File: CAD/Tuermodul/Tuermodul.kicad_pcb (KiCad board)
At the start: 2 copper layers, 206.1 x 101.6 mm, 174 parts, among them J101 Conn_02x16_Counter_Clockwise, J201 Conn_02x20_Odd_Even, J202 Conn_02x01, J203 Conn_02x01, J204 Conn_02x01, J205 Conn_02x01, J301 Conn_02x20_Counter_Clockwise, Q205 Q_NPN_CBE, Q206 Q_NPN_CBE, Q207 Q_NPN_CBE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

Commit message: -mod: DIN Stecker auf Typ D geändert. Layout angepasst und optimiert.
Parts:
- J101: footprint DIN41612_Connectors_custom:DIN41612_B_2x16_Horizontal_counter_clockwise -> DIN41612_Connectors_custom:DIN41612_D_32pol_90deg
- moved J101 39.0 mm to (67.2, 94.4), turned to 270 degrees
- moved R217 4.32 mm to (80.2, 122.4)
- moved R223 2.55 mm to (80.2, 120.8)
- moved C101 2.50 mm to (80.8, 59.7)
- moved C102 2.50 mm to (87.3, 59.7)
- moved C103 2.50 mm to (80.1, 89.3)
- moved C104 2.50 mm to (99.5, 87.9)
- moved C105 2.50 mm to (95.0, 81.3)
- moved C106 2.50 mm to (99.5, 97.0)
- moved C107 2.50 mm to (91.6, 73.2)
- moved C108 2.50 mm to (93.0, 81.3)
- moved C109 2.50 mm to (88.0, 73.2)
- moved C110 2.50 mm to (88.8, 81.3)
- moved C111 2.50 mm to (80.1, 96.4)
- moved C112 2.50 mm to (89.8, 101.0)
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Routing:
- net /~PWR_EN~: track 207.6 -> 185.5 mm
- net GND: track 58.5 -> 45.0 mm, vias 91 -> 85
- net /Error: track 180.9 -> 173.9 mm
- net Net-(J201-Pad6): track 142.8 -> 137.9 mm
- net Net-(J201-Pad7): track 113.9 -> 109.6 mm
- net Net-(J101-Pad13): track 26.2 -> 30.4 mm
- net /DoorC_MK: track 124.7 -> 121.1 mm
- net Net-(J101-Pad18): track 19.7 -> 16.3 mm, vias 0 -> 1
- net /DoorA_MK: track 154.2 -> 150.8 mm
- net Net-(J101-Pad8): track 8.66 -> 11.9 mm
- net Net-(J101-Pad7): track 7.92 -> 11.2 mm
- net /DoorD_VCC: track 103.8 -> 101.0 mm
- net Net-(J101-Pad12): track 22.7 -> 25.5 mm
- net /DoorD_MK: track 140.0 -> 137.4 mm
- net Net-(J201-Pad10): track 99.1 -> 96.6 mm
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
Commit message: -add: BOM -mod: letzte Schritte für LP Hersteller, Gerber Dateien für A0 generiert.
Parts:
- added R317: 0, Resistor_SMD:R_0603_1608Metric_Pad1.05x0.95mm_HandSolder, F.Cu at (222.2, 54.8)
- added R318: 0, Resistor_SMD:R_0603_1608Metric_Pad1.05x0.95mm_HandSolder, F.Cu at (222.2, 99.9)
- added R319: 0, Resistor_SMD:R_0603_1608Metric_Pad1.05x0.95mm_HandSolder, F.Cu at (222.2, 59.9)
- added R320: 0, Resistor_SMD:R_0603_1608Metric_Pad1.05x0.95mm_HandSolder, F.Cu at (222.2, 104.8)
- added R321: 0, Resistor_SMD:R_0603_1608Metric_Pad1.05x0.95mm_HandSolder, F.Cu at (222.2, 129.9)
- added R322: 0, Resistor_SMD:R_0603_1608Metric_Pad1.05x0.95mm_HandSolder, F.Cu at (222.2, 79.8)
- added R323: 0, Resistor_SMD:R_0603_1608Metric_Pad1.05x0.95mm_HandSolder, F.Cu at (222.2, 134.9)
- added R324: 0, Resistor_SMD:R_0603_1608Metric_Pad1.05x0.95mm_HandSolder, F.Cu at (222.2, 84.9)
- moved D310 12.5 mm to (252.7, 74.9)
- moved D323 12.5 mm to (252.7, 79.8)
- moved D324 12.5 mm to (252.7, 69.8)
- moved Q301 12.5 mm to (248.9, 55.3)
- moved R301 12.5 mm to (248.0, 47.7)
- moved R307 12.5 mm to (256.5, 89.2)
- moved R308 12.5 mm to (256.5, 84.5)
- moved R316 12.5 mm to (249.3, 113.0)
- moved R306 12.5 mm to (231.0, 65.9)
- moved R312 12.5 mm to (254.6, 101.0)
- moved D301 12.5 mm to (242.5, 54.5)
- moved D303 12.5 mm to (237.5, 49.5)
- moved D304 12.5 mm to (237.5, 54.5)
- moved D306 12.5 mm to (232.4, 74.9)
- moved D314 12.5 mm to (232.4, 110.4)
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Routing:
- net GNDA: track 0.00 -> 34.2 mm
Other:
- board size 206.1 x 101.6 mm -> 193.7 x 100 mm
- rule trace_min: 0.05 -> 0.089
- rule via_min_size: 0.4 -> 0.45

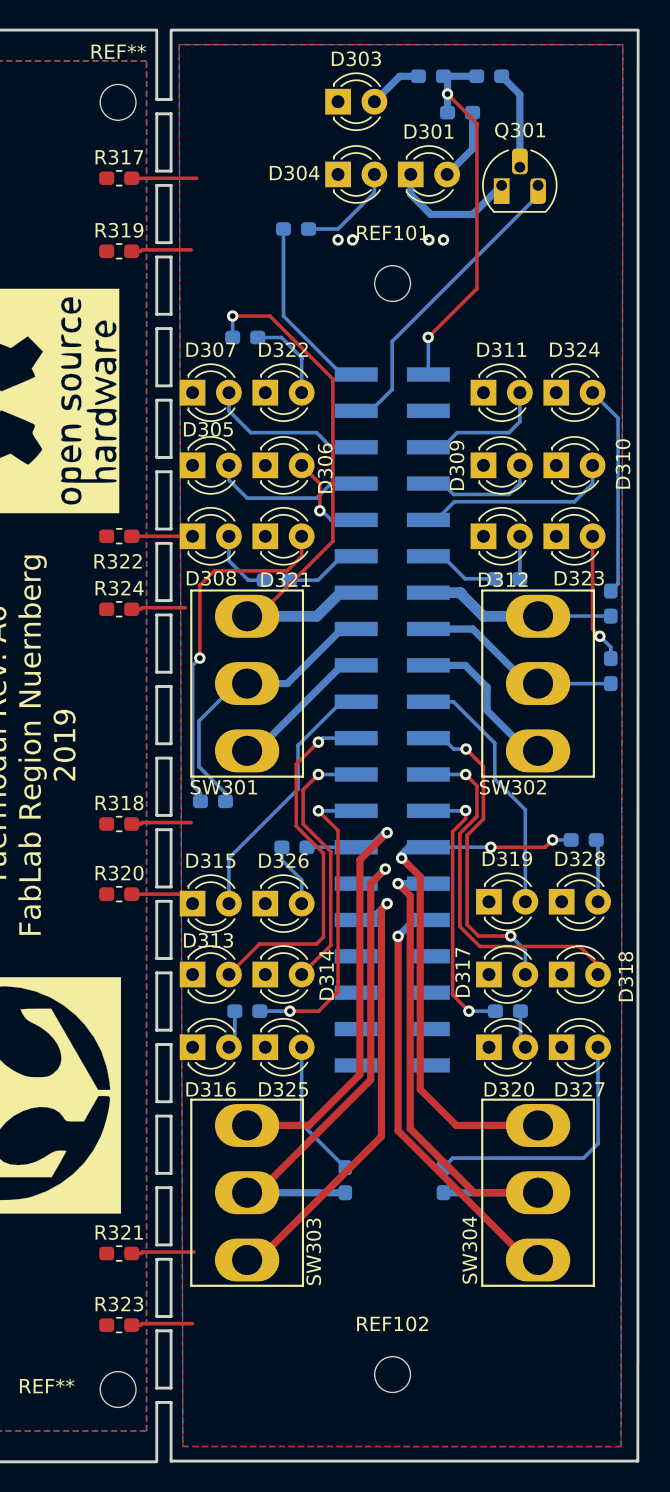
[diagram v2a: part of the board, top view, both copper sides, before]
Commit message: -mod: Front und Hauptplatine separiert -mod: BOM von Nicolas überarbeitet
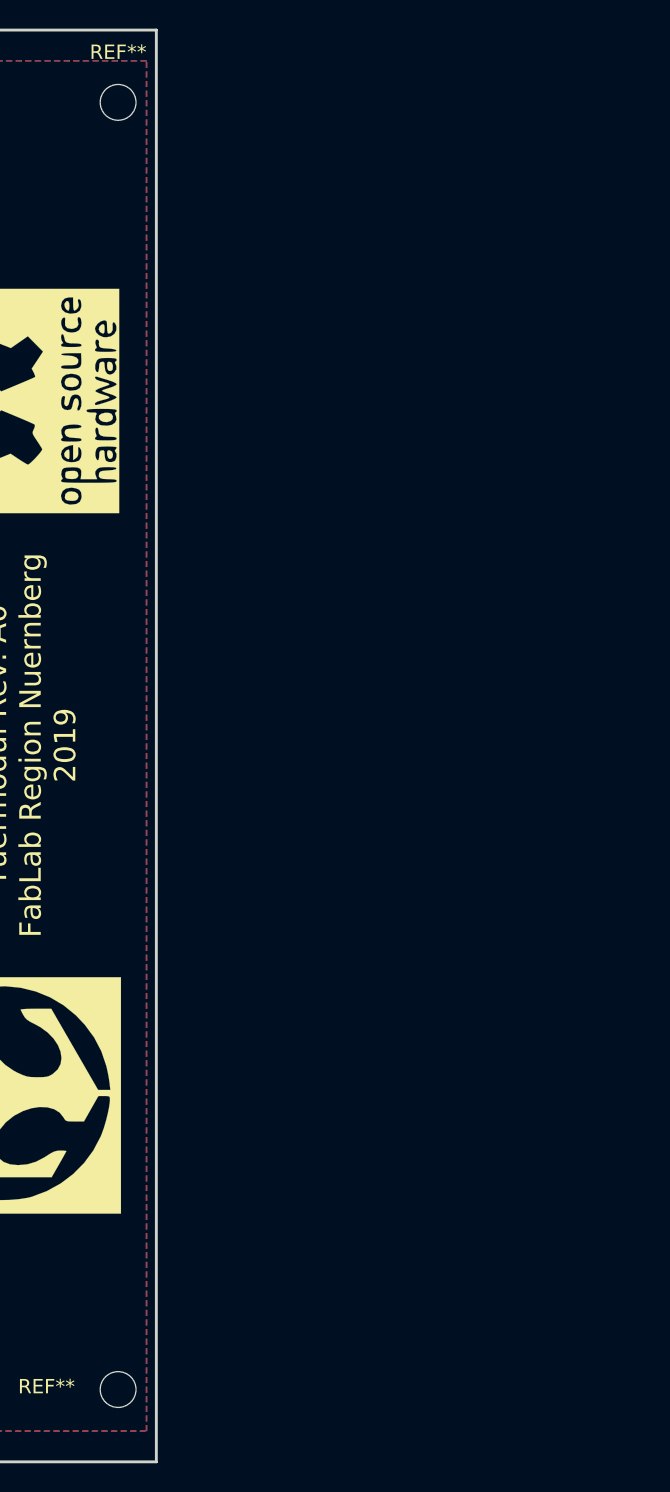
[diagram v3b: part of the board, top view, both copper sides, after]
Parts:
- removed D301, D303, D304, D305, D307, D308, D309, D311, D312, D313, D315, D316, D317, D319, D320, D321, D322, D323, D324, D325, D326, D327, D328: rt, LED_THT:LED_D3.0mm
- removed D306, D310, D314, D318: gn, LED_THT:LED_D3.0mm
- removed J301: Conn_02x20_Counter_Clockwise, Connector_PinSocket_2.54mm:PinSocket_2x20_P2.54mm_Vertical_SMD
- removed Q301: Q_NPN_CBE, Package_TO_SOT_THT:TO-92_HandSolder
- removed R301, R304: 1k, Resistor_SMD:R_0603_1608Metric_Pad1.05x0.95mm_HandSolder
- removed R302, R303: 330R, Resistor_SMD:R_0603_1608Metric_Pad1.05x0.95mm_HandSolder
- removed R305, R306, R307, R308, R309, R310, R311, R312: 4k7, Resistor_SMD:R_0603_1608Metric_Pad1.05x0.95mm_HandSolder
- removed R313, R314, R315, R316: 470R, Resistor_SMD:R_0603_1608Metric_Pad1.05x0.95mm_HandSolder
- removed R317, R318, R319, R320, R321, R322, R323, R324: 0, Resistor_SMD:R_0603_1608Metric_Pad1.05x0.95mm_HandSolder
- removed REF101, REF102: MountingHole_2.5mm, MountingHole:MountingHole_2.5mm
- removed SW301, SW302, SW303, SW304: SW_SPDT_MSM, Switches:SPDT
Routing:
- net /Front/DoorD_12V: track 39.6 -> 0.00 mm, vias 3 -> 0
- net /Front/DoorA_12V: track 39.4 -> 0.00 mm, vias 1 -> 0
- net /Front/DoorD_Lock: track 37.0 -> 0.00 mm, vias 1 -> 0
- net /Front/DoorC_Lock: track 36.4 -> 0.00 mm, vias 1 -> 0
- net GNDA: track 34.2 -> 0.00 mm, vias 4 -> 0
- net /Front/DoorC_12V: track 33.0 -> 0.00 mm, vias 1 -> 0
- net /Front/DoorC_Auto: track 32.0 -> 0.00 mm, vias 1 -> 0
- net /Front/DoorD_Auto: track 29.7 -> 0.00 mm, vias 1 -> 0
- net +5P: track 26.8 -> 0.00 mm, vias 2 -> 0
- net /Front/DC_Tx: track 25.5 -> 0.00 mm, vias 1 -> 0
- net /Front/DD_Rx: track 25.5 -> 0.00 mm, vias 1 -> 0
- net Net-(D321-Pad2): track 25.2 -> 0.00 mm, vias 1 -> 0
- net /Front/DD_Tx: track 22.7 -> 0.00 mm, vias 2 -> 0
- net /Front/DoorC_MK: track 21.9 -> 0.00 mm, vias 2 -> 0
- net /Front/Fuse_Error: track 21.6 -> 0.00 mm
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- removed copper zone on B.Cu, net GNDA
- removed copper zone on F.Cu, net GNDA
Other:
- board size 193.7 x 100 mm -> 160 x 100 mm
